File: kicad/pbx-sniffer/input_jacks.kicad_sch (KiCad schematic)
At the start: 24 parts

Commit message: picked new MCU and updated some part numbers
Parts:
- J1, J10, J11, J12, J13, J14, J15, J16, J17, J18, J19, J2, J20, J21, J22, J23, J24, J3, J4, J5, J6, J7, J8, J9: footprint (none) -> Phones:Molex 0955016649
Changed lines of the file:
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@@
 			)
 		)
-		(property "Footprint" ""
+		(property "Footprint" "Phones:Molex 0955016649"
 			(at 203.2 54.61 0)
 			(effects
@@
 			)
 		)
-		(property "Footprint" ""
+		(property "Footprint" "Phones:Molex 0955016649"
 			(at 81.28 54.61 0)
 			(effects
@@
 			)
 		)
-		(property "Footprint" ""
+		(property "Footprint" "Phones:Molex 0955016649"
 			(at 85.09 54.61 0)
 			(effects
@@
 			)
 		)
-		(property "Footprint" ""
+		(property "Footprint" "Phones:Molex 0955016649"
 			(at 81.28 95.25 0)
 			(effects
@@
 			)
 		)
-		(property "Footprint" ""
+		(property "Footprint" "Phones:Molex 0955016649"
 			(at 203.2 115.57 0)
 			(effects
@@
 			)
 		)
-		(property "Footprint" ""
+		(property "Footprint" "Phones:Molex 0955016649"
 			(at 85.09 74.93 0)
 			(effects
@@
 			)
 		)
-		(property "Footprint" ""
+		(property "Footprint" "Phones:Molex 0955016649"
 			(at 81.28 135.89 0)
 			(effects
@@
 			)
 		)
-		(property "Footprint" ""
+		(property "Footprint" "Phones:Molex 0955016649"
 			(at 203.2 95.25 0)
 			(effects
@@
 			)
 		)
-		(property "Footprint" ""
+		(property "Footprint" "Phones:Molex 0955016649"
 			(at 203.2 34.29 0)
 			(effects
@@
 			)
 		)
-		(property "Footprint" ""
+		(property "Footprint" "Phones:Molex 0955016649"
 			(at 85.09 115.57 0)
 			(effects
@@
 			)
 		)
-		(property "Footprint" ""
+		(property "Footprint" "Phones:Molex 0955016649"
 			(at 81.28 115.57 0)
 			(effects
@@
 			)
 		)
-		(property "Footprint" ""
+		(property "Footprint" "Phones:Molex 0955016649"
 			(at 199.39 135.89 0)
 			(effects
@@
 			)
 		)
-		(property "Footprint" ""
+		(property "Footprint" "Phones:Molex 0955016649"
 			(at 81.28 74.93 0)
 			(effects
@@
 			)
 		)
-		(property "Footprint" ""
+		(property "Footprint" "Phones:Molex 0955016649"
 			(at 199.39 34.29 0)
 			(effects
@@
 			)
 		)
-		(property "Footprint" ""
+		(property "Footprint" "Phones:Molex 0955016649"
 			(at 199.39 115.57 0)
 			(effects
@@
 			)
 		)
-		(property "Footprint" ""
+		(property "Footprint" "Phones:Molex 0955016649"
 			(at 85.09 95.25 0)
 			(effects
@@
 			)
 		)
-		(property "Footprint" ""
+		(property "Footprint" "Phones:Molex 0955016649"
 			(at 81.28 34.29 0)
 			(effects
@@
 			)
 		)
-		(property "Footprint" ""
+		(property "Footprint" "Phones:Molex 0955016649"
 			(at 199.39 74.93 0)
 			(effects
@@
 			)
 		)
-		(property "Footprint" ""
+		(property "Footprint" "Phones:Molex 0955016649"
 			(at 203.2 74.93 0)
 			(effects
@@
 			)
 		)
-		(property "Footprint" ""
+		(property "Footprint" "Phones:Molex 0955016649"
 			(at 85.09 135.89 0)
 			(effects
@@
 			)
 		)
-		(property "Footprint" ""
+		(property "Footprint" "Phones:Molex 0955016649"
 			(at 199.39 95.25 0)
 			(effects
@@
 			)
 		)
-		(property "Footprint" ""
+		(property "Footprint" "Phones:Molex 0955016649"
 			(at 203.2 135.89 0)
 			(effects
@@
 			)
 		)
-		(property "Footprint" ""
+		(property "Footprint" "Phones:Molex 0955016649"
 			(at 199.39 54.61 0)
 			(effects
@@
 			)
 		)
-		(property "Footprint" ""
+		(property "Footprint" "Phones:Molex 0955016649"
 			(at 85.09 34.29 0)
 			(effects

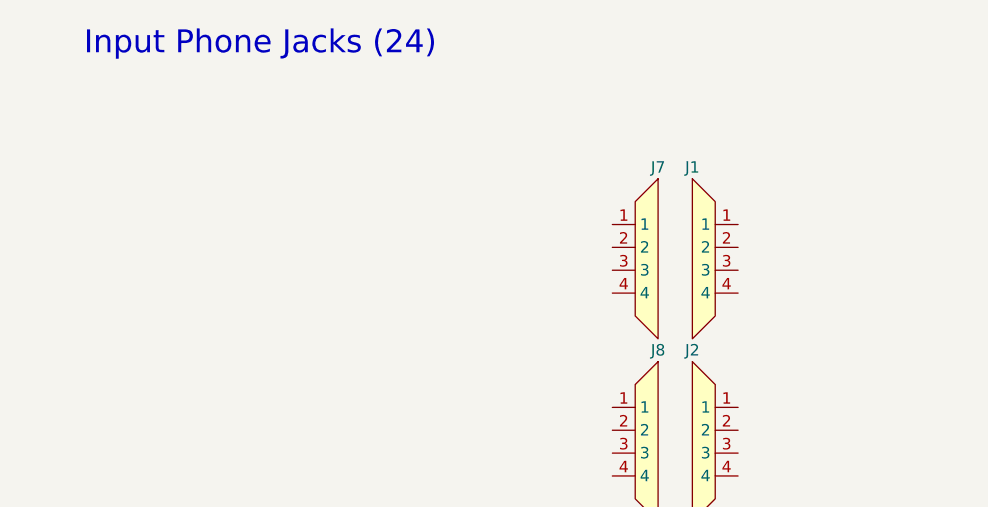
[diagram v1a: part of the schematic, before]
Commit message: drew schematic of naive wiretap circuit
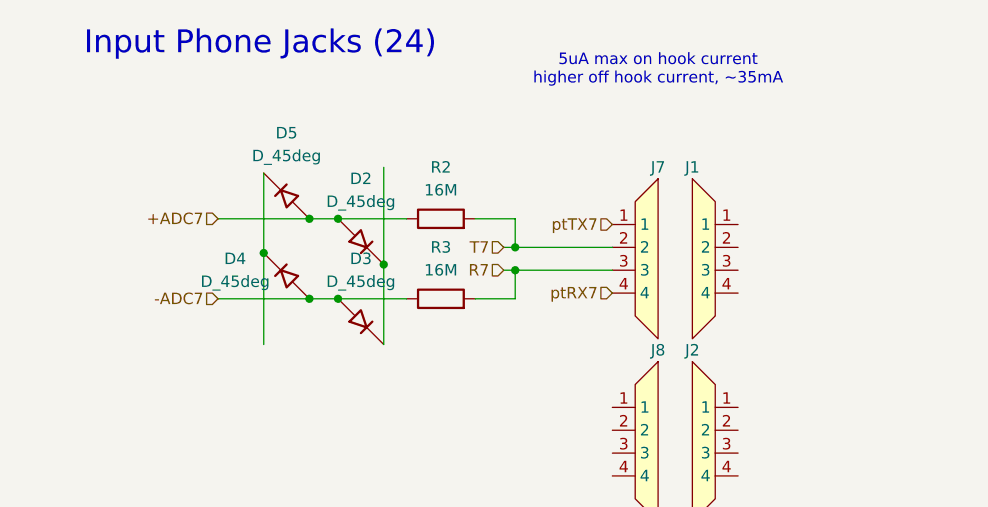
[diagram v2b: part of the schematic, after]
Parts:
- added D2, D3, D4, D5: D_45deg, symbol Device:D_45deg
- added R2, R3: 16M, symbol Device:R
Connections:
- net ptTX7: now reaches J7.1
- net T7: now reaches J7.2
- net T7: now also R2.2
- net R7: now reaches J7.3
- net R7: now also R3.2
- net ptRX7: now reaches J7.4
- new net: D2.1 (K), D3.1 (K)
- new net: D4.1 (K), D5.1 (K)
- new net +ADC7: D2.2 (A), D5.2 (A), R2.1
- new net -ADC7: D3.2 (A), D4.2 (A), R3.1
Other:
- note added: "5uA max on hook current higher off hook current, ~35mA"

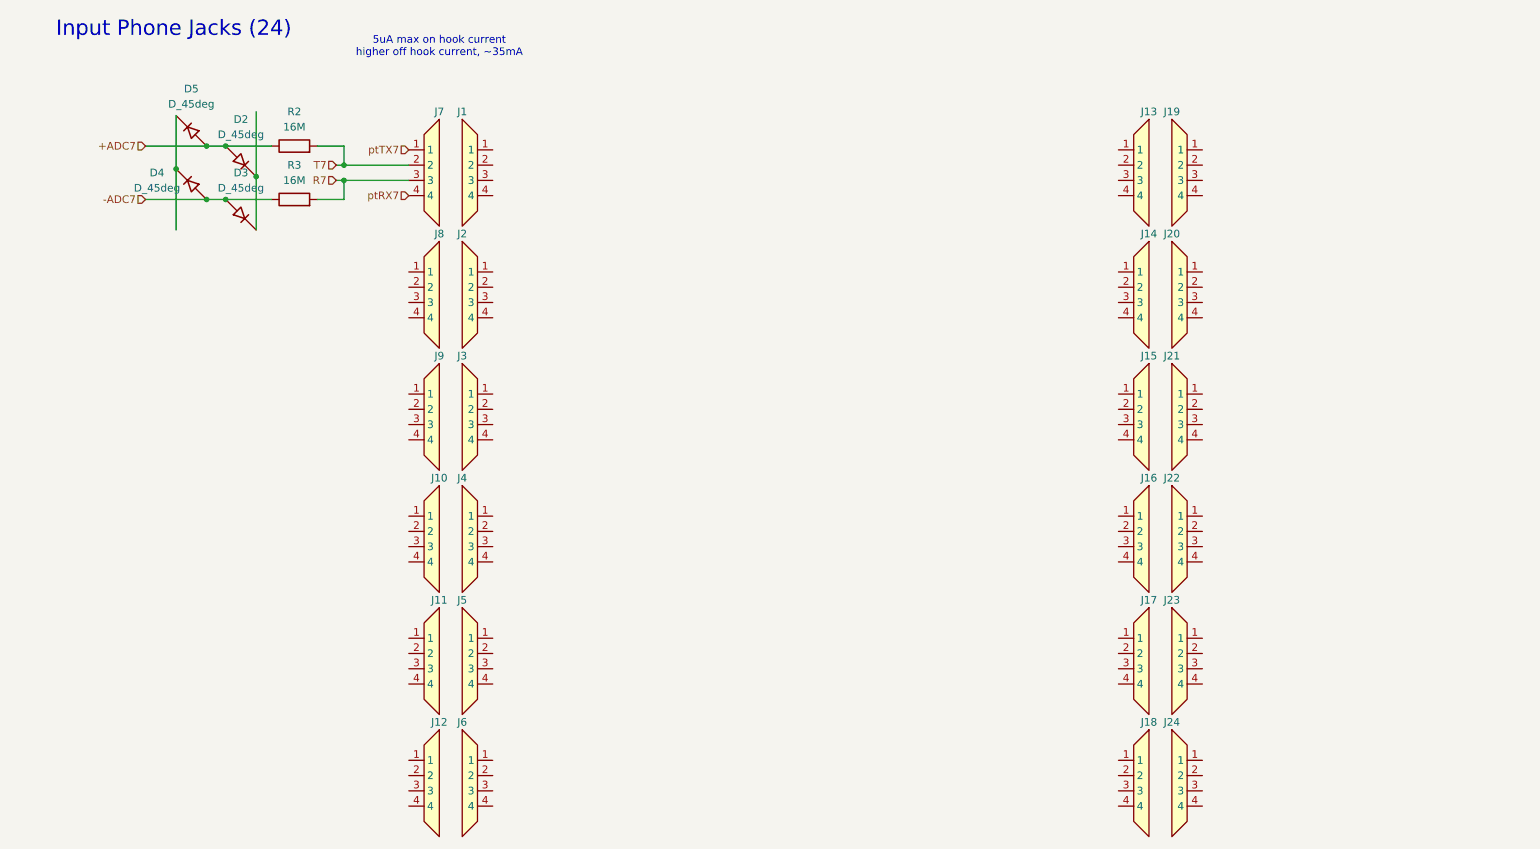
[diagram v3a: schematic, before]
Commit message: working on duplicating adc and control circuits between phone jacks
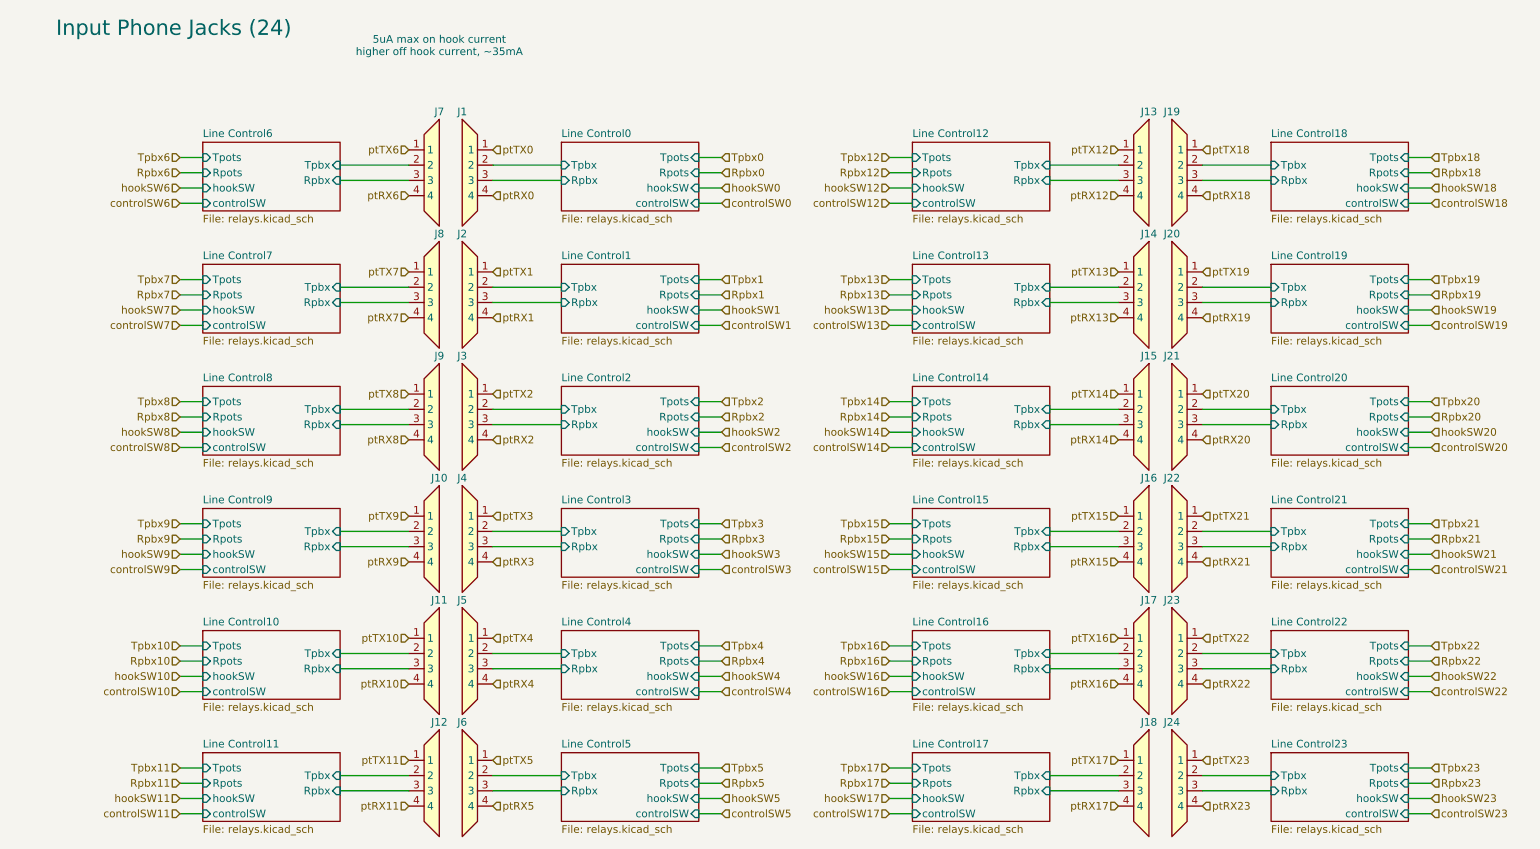
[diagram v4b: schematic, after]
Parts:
- removed D2, D3, D4, D5: D_45deg, symbol Device:D_45deg
- removed R2, R3: 16M, symbol Device:R
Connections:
- net ptRX7: now also J8.4; no longer J7.4
- net ptTX7: now also J8.1; no longer J7.1
- net ptTX19: now reaches J20.1
- net Line Control19/Tpbx: now reaches J20.2
- net Line Control19/Rpbx: now reaches J20.3
- net ptRX19: now reaches J20.4
- net Line Control7/Tpbx: now reaches J8.2
- net Line Control7/Rpbx: now reaches J8.3
- net ptTX1: now reaches J2.1
- net Line Control1/Tpbx: now reaches J2.2
- net Line Control1/Rpbx: now reaches J2.3
- net ptRX1: now reaches J2.4
- net ptTX9: now reaches J10.1
- net Line Control9/Tpbx: now reaches J10.2
- net Line Control9/Rpbx: now reaches J10.3
- net ptRX9: now reaches J10.4
- net ptTX22: now reaches J23.1
- net Line Control22/Tpbx: now reaches J23.2
- net Line Control22/Rpbx: now reaches J23.3
- net ptRX22: now reaches J23.4
- net ptTX2: now reaches J3.1
- net Line Control2/Tpbx: now reaches J3.2
- net Line Control2/Rpbx: now reaches J3.3
- net ptRX2: now reaches J3.4
- net ptTX11: now reaches J12.1
- net Line Control11/Tpbx: now reaches J12.2
- net Line Control11/Rpbx: now reaches J12.3
- net ptRX11: now reaches J12.4
- net ptTX21: now reaches J22.1
- net Line Control21/Tpbx: now reaches J22.2
- net Line Control21/Rpbx: now reaches J22.3
- net ptRX21: now reaches J22.4
- net ptTX18: now reaches J19.1
- net Line Control18/Tpbx: now reaches J19.2
- net Line Control18/Rpbx: now reaches J19.3
- net ptRX18: now reaches J19.4
- net ptTX4: now reaches J5.1
- net Line Control4/Tpbx: now reaches J5.2
- net Line Control4/Rpbx: now reaches J5.3
- net ptRX4: now reaches J5.4
- net ptTX10: now reaches J11.1
- net Line Control10/Tpbx: now reaches J11.2
- net Line Control10/Rpbx: now reaches J11.3
- net ptRX10: now reaches J11.4
- net ptTX17: now reaches J18.1
- net Line Control17/Tpbx: now reaches J18.2
- net Line Control17/Rpbx: now reaches J18.3
- net ptRX17: now reaches J18.4
- net ptTX8: now reaches J9.1
- net Line Control8/Tpbx: now reaches J9.2
- net Line Control8/Rpbx: now reaches J9.3
- net ptRX8: now reaches J9.4
- net ptTX12: now reaches J13.1
- net Line Control12/Tpbx: now reaches J13.2
- net Line Control12/Rpbx: now reaches J13.3
- net ptRX12: now reaches J13.4
- net ptTX16: now reaches J17.1
- net Line Control16/Tpbx: now reaches J17.2
- net Line Control16/Rpbx: now reaches J17.3
- net ptRX16: now reaches J17.4
- net ptTX3: now reaches J4.1
- net Line Control3/Tpbx: now reaches J4.2
- net Line Control3/Rpbx: now reaches J4.3
- net ptRX3: now reaches J4.4
- net ptTX14: now reaches J15.1
- net Line Control14/Tpbx: now reaches J15.2
- net Line Control14/Rpbx: now reaches J15.3
- net ptRX14: now reaches J15.4
- net ptTX20: now reaches J21.1
- net Line Control20/Tpbx: now reaches J21.2
- net Line Control20/Rpbx: now reaches J21.3
- net ptRX20: now reaches J21.4
- net ptTX5: now reaches J6.1
- net Line Control5/Tpbx: now reaches J6.2
- net Line Control5/Rpbx: now reaches J6.3
- net ptRX5: now reaches J6.4
- net ptTX15: now reaches J16.1
- net Line Control15/Tpbx: now reaches J16.2
- net Line Control15/Rpbx: now reaches J16.3
- net ptRX15: now reaches J16.4
- net ptTX23: now reaches J24.1
- net Line Control23/Tpbx: now reaches J24.2
- net Line Control23/Rpbx: now reaches J24.3
- net ptRX23: now reaches J24.4
- net ptTX13: now reaches J14.1
- net Line Control13/Tpbx: now reaches J14.2
- net Line Control13/Rpbx: now reaches J14.3
- net ptRX13: now reaches J14.4
- net ptTX0: now reaches J1.1
- net Line Control0/Tpbx: now reaches J1.2
- net Line Control0/Rpbx: now reaches J1.3
- net ptRX0: now reaches J1.4
- net R7 renamed Line Control6/Rpbx
- net T7 renamed Line Control6/Tpbx
- new net ptRX6: J7.4
- new net ptTX6: J7.1
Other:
- added sheet Line Control0 (relays.kicad_sch)
- added sheet Line Control1 (relays.kicad_sch)
- added sheet Line Control10 (relays.kicad_sch)
- added sheet Line Control11 (relays.kicad_sch)
- added sheet Line Control12 (relays.kicad_sch)
- added sheet Line Control13 (relays.kicad_sch)
- added sheet Line Control14 (relays.kicad_sch)
- added sheet Line Control15 (relays.kicad_sch)
- added sheet Line Control16 (relays.kicad_sch)
- added sheet Line Control17 (relays.kicad_sch)
- added sheet Line Control18 (relays.kicad_sch)
- added sheet Line Control19 (relays.kicad_sch)
- added sheet Line Control2 (relays.kicad_sch)
- added sheet Line Control20 (relays.kicad_sch)
- added sheet Line Control21 (relays.kicad_sch)
- added sheet Line Control22 (relays.kicad_sch)
- added sheet Line Control23 (relays.kicad_sch)
- added sheet Line Control3 (relays.kicad_sch)
- added sheet Line Control4 (relays.kicad_sch)
- added sheet Line Control5 (relays.kicad_sch)
- added sheet Line Control6 (relays.kicad_sch)
- added sheet Line Control7 (relays.kicad_sch)
- added sheet Line Control8 (relays.kicad_sch)
- added sheet Line Control9 (relays.kicad_sch)
